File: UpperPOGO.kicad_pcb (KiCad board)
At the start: 2 copper layers, 128 x 58.5 mm, 29 parts, among them J1 Conn_01x01_MountingPin, J10 Conn_01x01_MountingPin, J11 Conn_01x01_MountingPin, J12 Conn_01x01_MountingPin, J13 Conn_01x01_MountingPin, J14 Conn_01x01_MountingPin, J15 Conn_01x01_MountingPin, J16 Conn_01x01_MountingPin, J17 Conn_01x01_MountingPin, J18 Conn_01x01_MountingPin, J19 Conn_01x01_MountingPin, J2 Conn_01x01_MountingPin, J20 Conn_01x01_MountingPin, J21 Conn_01x01_MountingPin, J22 Conn_01x01_MountingPin, J23 Conn_01x01_MountingPin, J24 Conn_01x01_MountingPin, J25 Conn_01x24_Pin, J3 Conn_01x01_MountingPin, J4 Conn_01x01_MountingPin, J5 Conn_01x01_MountingPin, J6 Conn_01x01_MountingPin, J7 Conn_01x01_MountingPin, J8 Conn_01x01_MountingPin, J9 Conn_01x01_MountingPin

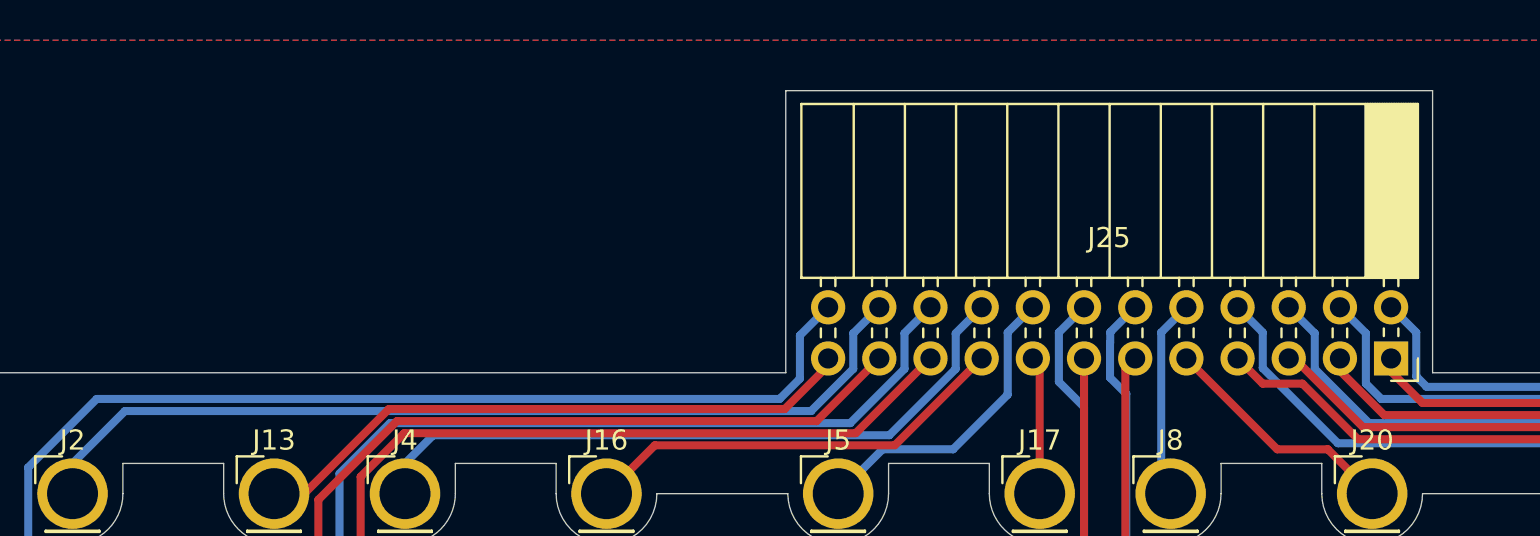
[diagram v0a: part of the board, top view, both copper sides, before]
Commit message: Update rev3 to modify J25 connector: Move J25 to be populated from the back of board Change J25 BOM to a straight connector (no right-angle)
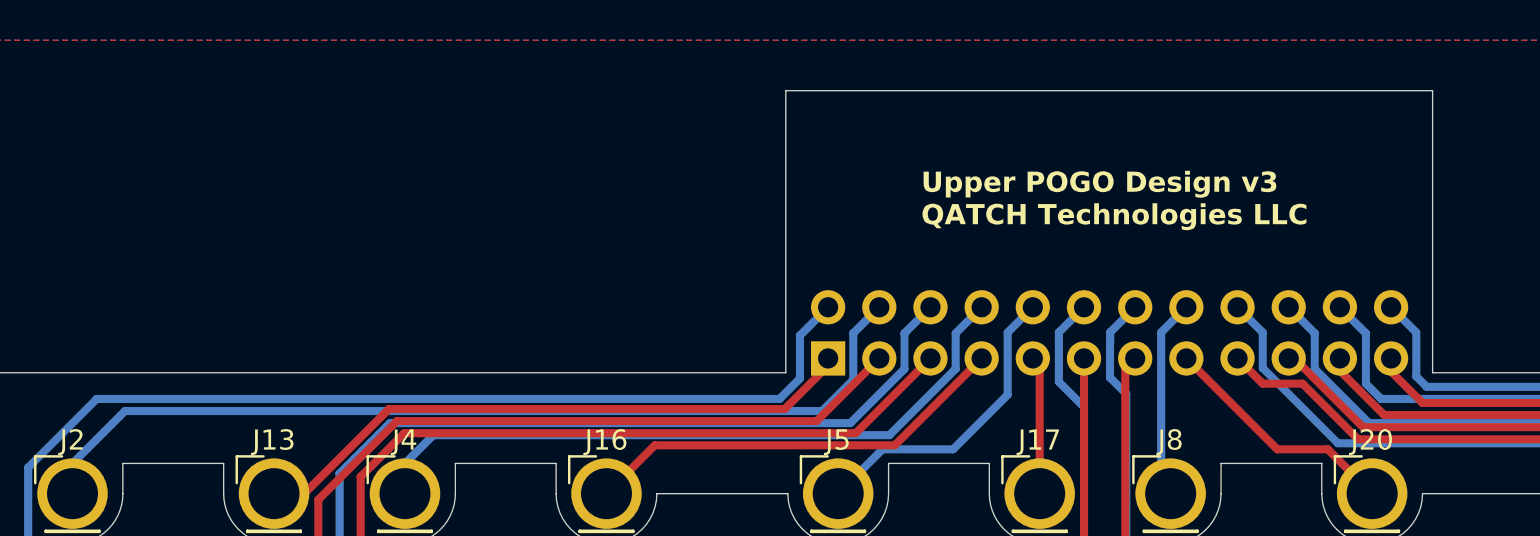
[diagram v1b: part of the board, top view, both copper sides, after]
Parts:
- J25: moved to B.Cu
- moved J25 0.84 mm to (147.1, 47.2), turned to 180 degrees
